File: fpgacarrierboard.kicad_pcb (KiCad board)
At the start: 6 copper layers, 150 x 100 mm, 215 parts, among them J1 Conn_01x06, J2 Conn_Coaxial, J3 HR911130C, J4 SFPK-SL, J5 Conn_02x10_Odd_Even, J6 Conn_01x04, SW1 SW_Push, SW2 SW_Push, SW3 SW_Push, U1 TPS62130A, U2 TPS62130A, U3 TPS62130A, U4 TPS62130A, U5 TPS2592xx, U6 XC7A35T-FGG484, U7 W25Q128JVS, U8 RTL8211E-VB-CG, U9 ESP32-C3-MINI-1-N4, Y1 OT322550MJBA4SL, Y3 OT322525MJBA4SL

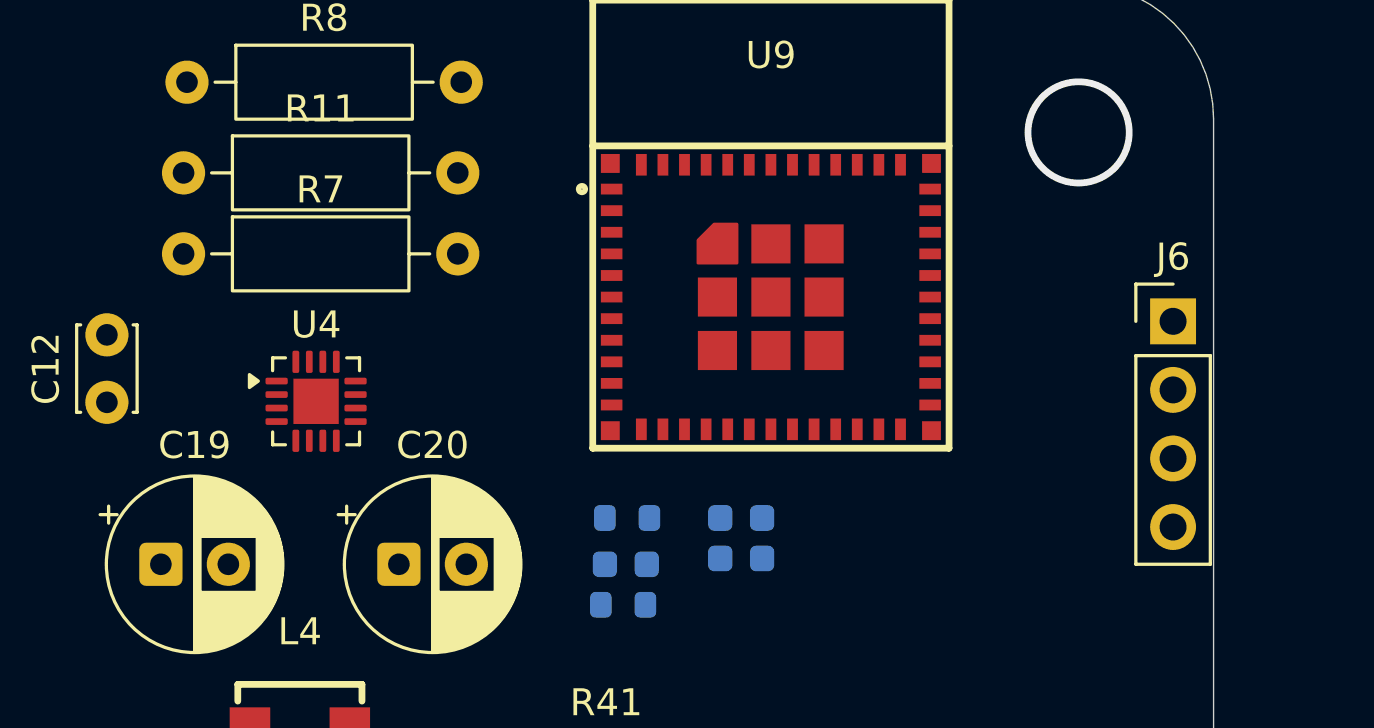
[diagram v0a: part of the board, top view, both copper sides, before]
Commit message: Board setup: JLC design rules, net classes, ENIG finish
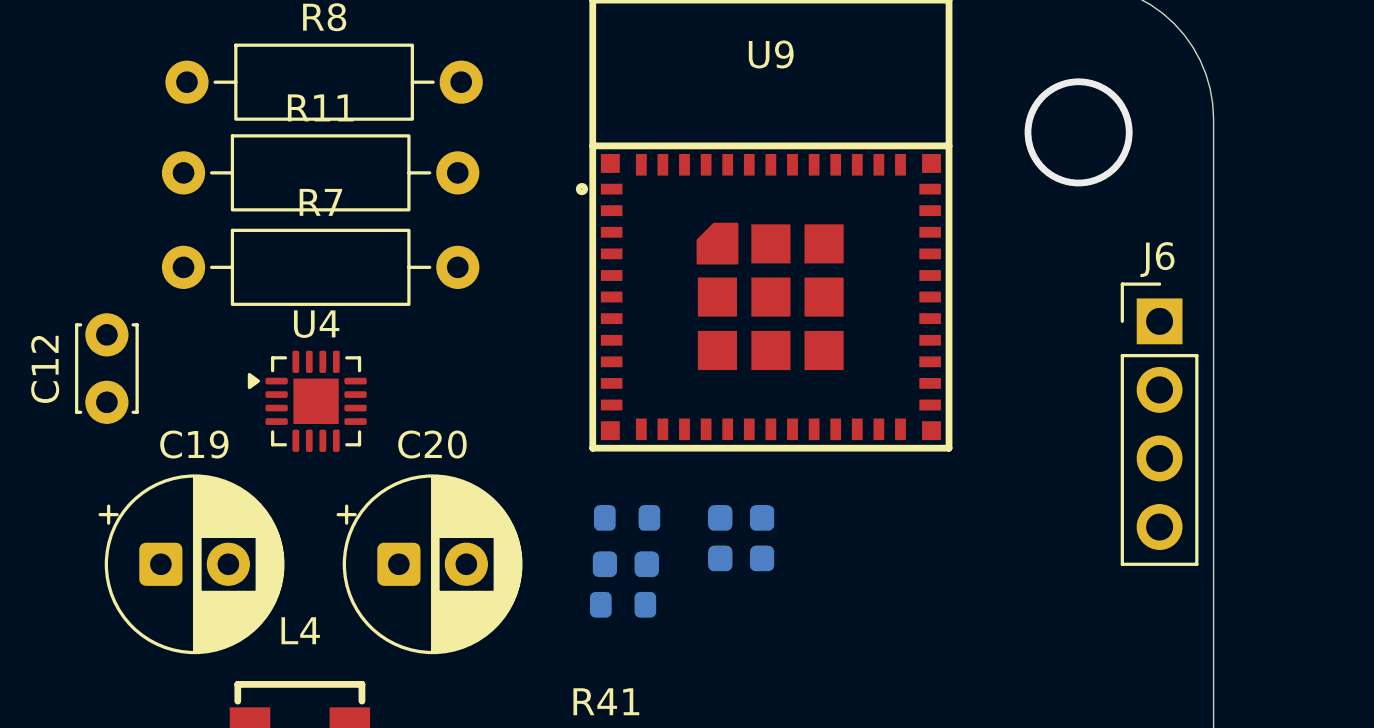
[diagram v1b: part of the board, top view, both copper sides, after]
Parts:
- moved J6 0.50 mm to (273.0, 37.0)
- moved R7 0.50 mm to (236.8, 35.0)
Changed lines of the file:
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@@
 				(type "Bottom Silk Screen")
 			)
-			(copper_finish "None")
+			(copper_finish "ENIG")
 			(dielectric_constraints yes)
 		)
 		(pad_to_mask_clearance 0)
+		(solder_mask_min_width 0.1)
 		(allow_soldermask_bridges_in_footprints no)
 		(tenting
@@
 		(capping no)
 		(filling no)
+		(zone_defaults)
 		(pcbplotparams
 			(layerselection 0x00000000_00000000_55555555_5755f5ff)
@@
 	(footprint "Connector_PinHeader_2.54mm:PinHeader_1x04_P2.54mm_Vertical"
 		(layer "F.Cu")
-		(at 273.5 37)
+		(at 273 37)
 		(descr "Through hole straight pin header, 1x04, 2.54mm pitch, single row")
 		(tags "Through hole pin header THT 1x04 2.54mm single row")
@@
 	(footprint "Resistor_THT:R_Axial_DIN0207_L6.3mm_D2.5mm_P10.16mm_Horizontal"
 		(layer "F.Cu")
-		(at 236.84 34.5)
+		(at 236.84 35)
 		(descr "Resistor, Axial_DIN0207 series, Axial, Horizontal, pin pitch=10.16mm, 0.25W = 1/4W, length*diameter=6.3*2.5mm^2, http://cdn-reichelt.de/documents/datenblatt/B400/1_4W%23YAG.pdf")
 		(tags "Resistor Axial_DIN0207 series Axial Horizontal pin pitch 10.16mm 0.25W = 1/4W length 6.3mm diameter 2.5mm")

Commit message: Remove optional WiFi sheet from schematic and PCB
- Delete wifi sheet and its seven parts; restore no-connect flags on the five freed FPGA bank-34 pins
- Reduce J4 pad solder-mask margin so the fine-pitch pads meet the 0.1mm web rule
- Regenerate BOM and ERC report
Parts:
- removed C115, C116: 0.1uF, Capacitor_SMD:C_0603_1608Metric
- removed C117: 22uF, Capacitor_SMD:C_0603_1608Metric
- removed J6: Conn_01x04, Connector_PinHeader_2.54mm:PinHeader_1x04_P2.54mm_Vertical
- removed R52, R53: 10k, Resistor_SMD:R_0603_1608Metric
- removed U9: ESP32-C3-MINI-1-N4, easyeda:WIFIM-SMD_ESP32-C3-MINI-1

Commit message: Pre-routing checkpoint: zone pours, net labels, decoupling on bottom, R51 1k
- GND pours on F.Cu, In1.Cu, In4.Cu, B.Cu; In3.Cu power pours for 1V0, 1V8,
  5V_LC, MGTAVCC, MGTAVTT, 3V3 (3V3 lowest priority)
- Local labels on previously unnamed power nets
- FPGA decoupling moved to B.Cu under/around U6
- R51 (PUDC_B pull-up) 4.7k -> 1k per UG470
- Silkscreen cleanup
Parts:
- R51: value 4.7k -> 1k
- TP5: value TestPoint -> 5V_LC_TP
- moved R23 25.7 mm to (233.8, 61.5)
- moved R41 19.9 mm to (257.8, 36.5)
- moved R42 18.3 mm to (257.8, 42.5)
- moved C106 18.1 mm to (156.5, 106.0)
- moved C23 11.9 mm to (156.5, 111.0)
- moved C3 6.80 mm to (213.5, 110.5)
- moved R40 6.06 mm to (257.9, 48.5)
- moved C2 5.50 mm to (220.0, 110.5)
- moved R43 3.96 mm to (257.9, 55.5)
- moved R44 3.42 mm to (257.8, 62.0)
- moved SW1 3.00 mm to (268.4, 111.0)
- moved SW2 3.00 mm to (268.5, 101.0)
- moved SW3 3.00 mm to (268.5, 91.0)
- moved U6 3.00 mm to (201.5, 74.0)
- moved C8 2.98 mm to (220.0, 99.5)
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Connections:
- net Net-(J2-In) renamed /Clocks/PPS_SMA
- net Net-(L1-Pad2) renamed /Power_Rails/SW_1V0
- net Net-(L2-Pad2) renamed /Power_Rails/SW_1V8
- net Net-(L3-Pad2) renamed /Power_Rails/SW_1V2
- net Net-(L4-Pad2) renamed /Power_Rails/SW_3V3
- net Net-(OSC1-OUT+) renamed /Clocks/REFCLK_OSC_P
- net Net-(OSC1-OUT-) renamed /Clocks/REFCLK_OSC_N
- net Net-(U1-FB) renamed /Power_Rails/FB_1V0
- net Net-(U1-SS/TR) renamed /Power_Rails/SS_1V0
- net Net-(U2-FB) renamed /Power_Rails/FB_1V8
- net Net-(U2-SS/TR) renamed /Power_Rails/SS_1V8
- net Net-(U3-FB) renamed /Power_Rails/FB_1V2
- net Net-(U3-SS/TR) renamed /Power_Rails/SS_1V2
- net Net-(U4-FB) renamed /Power_Rails/FB_3V3
- net Net-(U4-SS/TR) renamed /Power_Rails/SS_3V3
- net Net-(U8-RSET) renamed /Ethernet_1G/PHY_RSET
- net Net-(USB1-CC1) renamed /PowerIn/USB_CC1
- net Net-(USB1-CC2) renamed /PowerIn/USB_CC2
- net Net-(Y1-OUT) renamed /Clocks/SYS_CLK_RAW
- U6 pad AA4: WIFI_MISO -> unconnected-(U6C-IO_L11N_T1_SRCC_34-PadAA4)
- U6 pad AA5: WIFI_MOSI -> unconnected-(U6C-IO_L10P_T1_34-PadAA5)
- U6 pad AB5: WIFI_SCLK -> unconnected-(U6C-IO_L10N_T1_34-PadAB5)
- U6 pad W4: WIFI_INT -> unconnected-(U6C-IO_L12N_T1_MRCC_34-PadW4)
- U6 pad Y4: WIFI_CS -> unconnected-(U6C-IO_L11P_T1_SRCC_34-PadY4)
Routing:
- added copper zone on In3.Cu, net 1V0
- added copper zone on In3.Cu, net 1V8
- added copper zone on In3.Cu, net 3V3
- added copper zone on In3.Cu, net 5V_LC
- added copper zone on B.Cu, net GND
- added copper zone on F.Cu, net GND
- added copper zone on In1.Cu, net GND
- added copper zone on In4.Cu, net GND
- added copper zone on In3.Cu, net MGTAVCC
- added copper zone on In3.Cu, net MGTAVTT

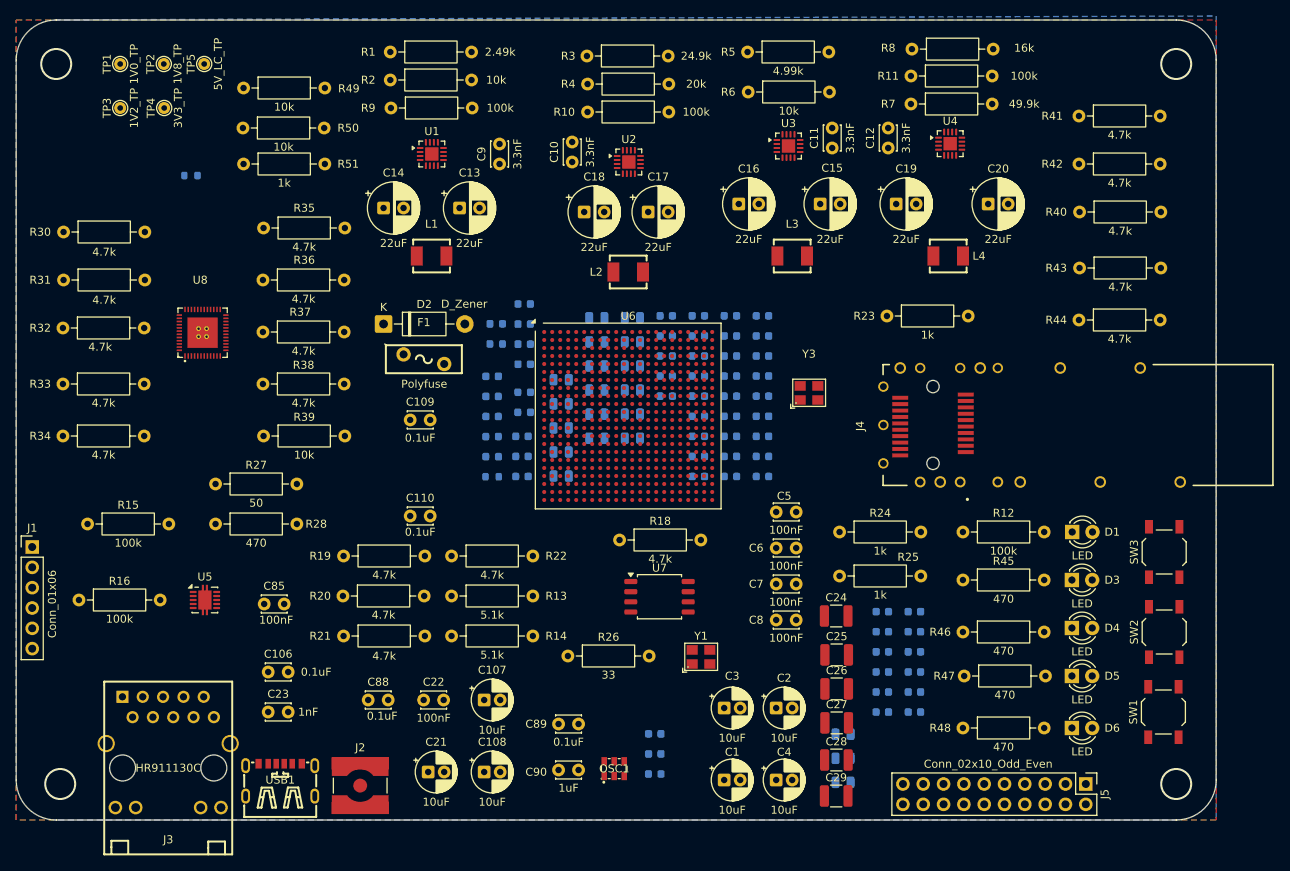
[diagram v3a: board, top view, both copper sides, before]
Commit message: Routing in progress: In3 power pours, DONE LED, DRC cleanup
- Add CFG_DONE 330R pull-up (R52) and DONE LED (D7, R53) per UG470
- Redraw In3.Cu pours to sit under their U6 balls (1V0 core, 1V8 strip,
  MGTAVCC, MGTAVTT); trim 5V_LC strip to y=50; zone clearance 0.2mm
- Remove 3V3/5V_LC traces from In4.Cu GND plane
- Custom rules: U6 BGA escape, solid GND on regulators/tight caps,
  1-spoke thermals on J4 and C22
- Fix clearance violations, remove dangling vias and stubs
- Remaining: GND pours split on In1.Cu/B.Cu by signal traces on In1.Cu
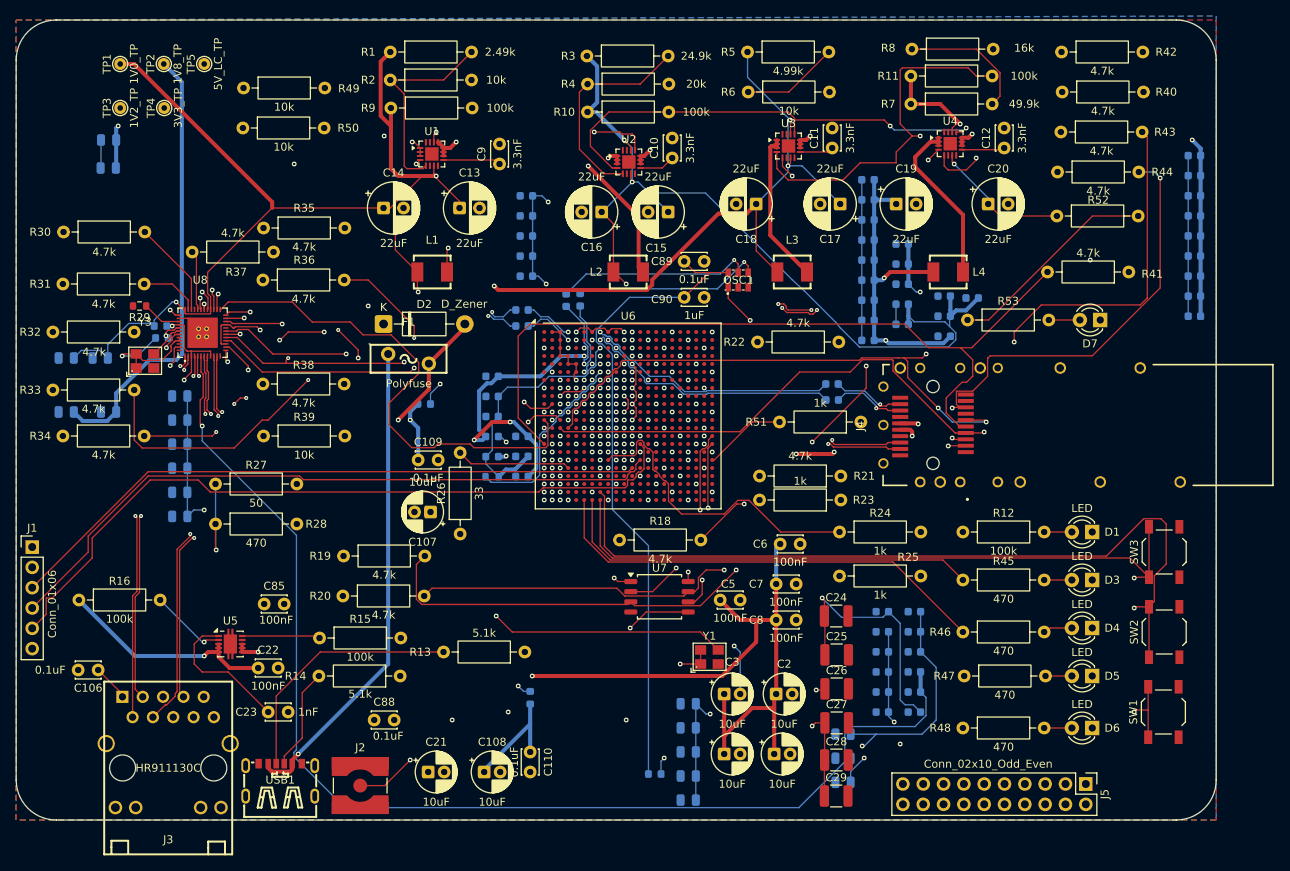
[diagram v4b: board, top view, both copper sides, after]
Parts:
- added D7: LED, LED_THT:LED_D3.0mm, F.Cu at (260.5, 62.0)
- added R52: 330, Resistor_THT:R_Axial_DIN0207_L6.3mm_D2.5mm_P10.16mm_Horizontal, F.Cu at (255.1, 49.0)
- added R53: 470, Resistor_THT:R_Axial_DIN0207_L6.3mm_D2.5mm_P10.16mm_Horizontal, F.Cu at (243.9, 62.0)
- R29: moved to F.Cu
- moved R51 83.6 mm to (230.6, 74.8), turned to 180 degrees
- moved Y3 83.1 mm to (141.1, 67.1)
- moved C34 73.9 mm to (136.6, 39.5)
- moved C35 73.7 mm to (136.5, 43.0)
- moved C32 71.0 mm to (131.2, 73.5)
- moved C31 70.8 mm to (131.2, 66.8)
- moved C30 66.7 mm to (135.5, 66.8)
- moved C33 65.5 mm to (136.6, 73.5)
- moved R21 65.3 mm to (228.1, 81.5), turned to 180 degrees
- moved C66 65.2 mm to (272.3, 44.0)
- moved C67 65.2 mm to (272.3, 46.5)
- moved C68 65.2 mm to (272.3, 49.0)
- moved C70 65.2 mm to (272.3, 54.0)
- moved C71 65.2 mm to (272.3, 56.5)
- moved C73 65.2 mm to (272.3, 61.5)
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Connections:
- net /Power_Rails/FB_1V0 renamed Net-(U1-FB)
- net /Power_Rails/SS_1V0 renamed Net-(U1-SS/TR)
- net /Power_Rails/SW_1V0 renamed Net-(L1-Pad2)
- U6 pad G11: unconnected-(U6F-DONE_0-PadG11) -> CFG_DONE
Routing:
- net 1V8: track 0.00 -> 294.1 mm, vias 0 -> 11
- net 1V0: track 0.00 -> 287.6 mm, vias 0 -> 26
- net BTN0: track 0.00 -> 229.2 mm, vias 0 -> 1
- net 3V3: track 0.00 -> 226.8 mm, vias 0 -> 60
- net BTN1: track 0.00 -> 215.2 mm, vias 0 -> 1
- net 5V_LC: track 0.00 -> 211.0 mm, vias 0 -> 7
- net 1V2: track 0.00 -> 199.8 mm, vias 0 -> 4
- net PHY_AVDD33: track 0.00 -> 168.8 mm, vias 0 -> 2
- net PHY_AVDD10: track 0.00 -> 161.5 mm, vias 0 -> 3
- net SFP_MODABS: track 0.00 -> 136.7 mm, vias 0 -> 3
- net SFP_SDA: track 0.00 -> 136.2 mm, vias 0 -> 1
- net SFP_TXFAULT: track 0.00 -> 120.5 mm, vias 0 -> 3
- net HDR_9: track 0.00 -> 114.9 mm, vias 0 -> 1
- net JTAG_TMS: track 0.00 -> 109.0 mm, vias 0 -> 1
- net 5V_FUSED: track 0.00 -> 108.0 mm, vias 0 -> 2
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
